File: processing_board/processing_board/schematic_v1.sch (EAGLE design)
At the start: 46 parts, among them Q1 BSS138, Q2 BSS138, Q3 BSS138, Q4 BSS138

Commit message: updated board
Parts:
- R13, R14, R15, R16, R17, R5, R6, R7, R8: value 10K -> 10k; device SparkFun-Resistors:220KOHM-0402T-1/16W-1% -> SparkFun-Resistors:10KOHM-0603-1/10W-1%
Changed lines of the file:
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@@
 <part name="D2" library="SparkFun-LED" deviceset="LED-GREEN" device="0603" value="GREEN"/>
 <part name="D3" library="SparkFun-LED" deviceset="LED-BLUE" device="0603" value="BLUE"/>
-<part name="R5" library="SparkFun-Resistors" deviceset="220KOHM" device="-0402T-1/16W-1%" value="10K"/>
-<part name="R6" library="SparkFun-Resistors" deviceset="220KOHM" device="-0402T-1/16W-1%" value="10K"/>
-<part name="R7" library="SparkFun-Resistors" deviceset="220KOHM" device="-0402T-1/16W-1%" value="10K"/>
+<part name="R5" library="SparkFun-Resistors" deviceset="10KOHM" device="-0603-1/10W-1%" value="10k"/>
+<part name="R6" library="SparkFun-Resistors" deviceset="10KOHM" device="-0603-1/10W-1%" value="10k"/>
+<part name="R7" library="SparkFun-Resistors" deviceset="10KOHM" device="-0603-1/10W-1%" value="10k"/>
 <part name="GND9" library="supply" deviceset="GND" device=""/>
 <part name="D4" library="SparkFun-LED" deviceset="LED-RED" device="0603" value="RED"/>
-<part name="R8" library="SparkFun-Resistors" deviceset="220KOHM" device="-0402T-1/16W-1%" value="10K"/>
+<part name="R8" library="SparkFun-Resistors" deviceset="10KOHM" device="-0603-1/10W-1%" value="10k"/>
 <part name="GND10" library="supply" deviceset="GND" device=""/>
 <part name="GND11" library="supply" deviceset="GND" device=""/>
@@
 <part name="PWR13" library="supply" deviceset="+5V" device=""/>
 <part name="D5" library="SparkFun-LED" deviceset="LED-GREEN" device="0603" value="GREEN"/>
-<part name="R13" library="SparkFun-Resistors" deviceset="220KOHM" device="-0402T-1/16W-1%" value="10K"/>
+<part name="R13" library="SparkFun-Resistors" deviceset="10KOHM" device="-0603-1/10W-1%" value="10k"/>
 <part name="PWR14" library="supply" deviceset="+3.3V" device=""/>
 <part name="PWR15" library="supply" deviceset="+5V" device=""/>
 <part name="D6" library="SparkFun-LED" deviceset="LED-GREEN" device="0603" value="GREEN"/>
-<part name="R14" library="SparkFun-Resistors" deviceset="220KOHM" device="-0402T-1/16W-1%" value="10K"/>
+<part name="R14" library="SparkFun-Resistors" deviceset="10KOHM" device="-0603-1/10W-1%" value="10k"/>
 <part name="D7" library="SparkFun-LED" deviceset="LED-GREEN" device="0603" value="GREEN"/>
-<part name="R15" library="SparkFun-Resistors" deviceset="220KOHM" device="-0402T-1/16W-1%" value="10K"/>
+<part name="R15" library="SparkFun-Resistors" deviceset="10KOHM" device="-0603-1/10W-1%" value="10k"/>
 <part name="PWR16" library="supply" deviceset="+3.3V" device=""/>
-<part name="R16" library="SparkFun-Resistors" deviceset="220KOHM" device="-0402T-1/16W-1%" value="10K"/>
+<part name="R16" library="SparkFun-Resistors" deviceset="10KOHM" device="-0603-1/10W-1%" value="10k"/>
 <part name="D8" library="SparkFun-LED" deviceset="LED-GREEN" device="0603" value="GREEN"/>
-<part name="R17" library="SparkFun-Resistors" deviceset="220KOHM" device="-0402T-1/16W-1%" value="10K"/>
+<part name="R17" library="SparkFun-Resistors" deviceset="10KOHM" device="-0603-1/10W-1%" value="10k"/>
 <part name="GND12" library="supply" deviceset="GND" device=""/>
 <part name="GND13" library="supply" deviceset="GND" device=""/>

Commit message: new teensy 4.1 footprint
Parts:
- removed U$1: DEV-16771, teensy_4_1:DEV-16771
- added B1: ARDUINO_UNO_R3, SparkFun-Boards:ARDUINO_UNO_R3
- added U$4: TEENSY41-E, teensy:TEENSY41-E
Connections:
- removed net N$9: JP1.10, U$1.D33
- new net N$15: U$4.37-PWM
- net +5V: now also U$4.VIN; no longer U$1.VIN
- net GND: now also U$4.5V, U$4.GND1, U$4.GND2, U$4.GND3, U$4.GND4, U$4.GND5, U$4.GND6; no longer U$1.AGND, U$1.GND, U$1.GND@1
- net N$1: now also U$4.35/TX8; no longer U$1.D35
- net N$11: now also U$4.1-TX1/MISO1/CTX2; no longer U$1.D1
- net N$2: now also U$4.34-RX8; no longer U$1.D34
- net N$5: now also U$4.0-RX1/CS1/CRX2; no longer U$1.D0
- net RESET_: now also JP1.10, U$4.33-MCLK2; no longer U$1.D36
- net SCL: now also U$4.16-A2/RX4/SCL1; no longer U$1.D19/A6
- net SDA: now also U$4.17-A3/TX4/SDA1; no longer U$1.D18/A5
- net TEENSY_3.3V: no longer U$1.3.3V
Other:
- moved on the sheet: C1, C2, C3, C4, C5, C6, D1, D2, D3, D4, D5, D8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

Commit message: pushing
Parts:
- added J5: (no value), SparkFun-Connectors:CONN_02
- added R18: 10k, SparkFun-Resistors:10KOHM-0603-1/10W-1%
- added R19: 8.2k, SparkFun-Resistors:8.2KOHM-0603-1/10W-5%
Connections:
- new net POWER_DIVIDED: R18.1, R19.2, U$4.27-A13/SCK1
- net +15V: now also R18.2
- net +5V: now also B1.VIN
- net CAN_RX1: now also J5.1
- net CAN_TX1: now also J5.2
- net GND: now also B1.GND, R19.1
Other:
- moved on the sheet: B1
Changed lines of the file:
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@@
 <part name="U$4" library="teensy" deviceset="TEENSY41-E" device=""/>
 <part name="B1" library="SparkFun-Boards" deviceset="ARDUINO_UNO_R3" device=""/>
+<part name="GND4" library="supply" deviceset="GND" device=""/>
+<part name="R18" library="SparkFun-Resistors" deviceset="10KOHM" device="-0603-1/10W-1%" value="10k"/>
+<part name="R19" library="SparkFun-Resistors" deviceset="8.2KOHM" device="-0603-1/10W-5%" value="8.2k"/>
+<part name="GND16" library="supply" deviceset="GND" device=""/>
+<part name="J5" library="SparkFun-Connectors" deviceset="CONN_02" device=""/>
 </parts>
 <sheets>
@@
 <instance part="GND15" gate="VR1" x="-147.32" y="-30.48" smashed="yes" rot="MR0"/>
 <instance part="U$4" gate="G$1" x="25.4" y="35.56" smashed="yes" rot="MR0"/>
-<instance part="B1" gate="G$1" x="142.24" y="-45.72" smashed="yes">
-<attribute name="NAME" x="132.588" y="-14.478" size="1.778" layer="95" font="vector"/>
-<attribute name="VALUE" x="132.08" y="-76.454" size="1.778" layer="96" font="vector" align="top-left"/>
+<instance part="B1" gate="G$1" x="142.24" y="58.42" smashed="yes">
+<attribute name="NAME" x="132.588" y="89.662" size="1.778" layer="95" font="vector"/>
+<attribute name="VALUE" x="132.08" y="27.686" size="1.778" layer="96" font="vector" align="top-left"/>
+</instance>
+<instance part="GND4" gate="VR1" x="116.84" y="30.48" smashed="yes" rot="R270"/>
+<instance part="R18" gate="G$1" x="137.16" y="165.1" smashed="yes" rot="R90">
+<attribute name="NAME" x="135.636" y="165.1" size="1.778" layer="95" font="vector" rot="R90" align="bottom-center"/>
+<attribute name="VALUE" x="138.684" y="165.1" size="1.778" layer="96" font="vector" rot="R90" align="top-center"/>
+</instance>
+<instance part="R19" gate="G$1" x="137.16" y="147.32" smashed="yes" rot="R90">
+<attribute name="NAME" x="135.636" y="147.32" size="1.778" layer="95" font="vector" rot="R90" align="bottom-center"/>
+<attribute name="VALUE" x="138.684" y="147.32" size="1.778" layer="96" font="vector" rot="R90" align="top-center"/>
+</instance>
+<instance part="GND16" gate="VR1" x="137.16" y="137.16" smashed="yes"/>
+<instance part="J5" gate="G$1" x="325.12" y="55.88" smashed="yes" rot="R180">
+<attribute name="VALUE" x="327.66" y="60.706" size="1.778" layer="96" font="vector" rot="R180"/>
+<attribute name="NAME" x="327.66" y="50.292" size="1.778" layer="95" font="vector" rot="R180"/>
 </instance>
 </instances>
@@
 <wire x1="-175.26" y1="-22.86" x2="-185.42" y2="-22.86" width="0.1524" layer="91"/>
 </segment>
+<segment>
+<pinref part="GND4" gate="VR1" pin="GND"/>
+<wire x1="119.38" y1="30.48" x2="129.54" y2="30.48" width="0.1524" layer="91"/>
+<label x="119.38" y="25.4" size="1.778" layer="95" rot="R180"/>
+<wire x1="129.54" y1="30.48" x2="130.81" y2="30.48" width="0.1524" layer="91"/>
+<junction x="129.54" y="30.48"/>
+<pinref part="B1" gate="G$1" pin="GND"/>
+</segment>
+<segment>
+<pinref part="GND16" gate="VR1" pin="GND"/>
+<wire x1="137.16" y1="142.24" x2="137.16" y2="139.7" width="0.1524" layer="91"/>
+<pinref part="R19" gate="G$1" pin="1"/>
+</segment>
 </net>
 <net name="+15V" class="0">
@@
 <wire x1="104.14" y1="167.64" x2="99.06" y2="167.64" width="0.1524" layer="91" grouprefs="POWER"/>
 <wire x1="99.06" y1="167.64" x2="99.06" y2="172.72" width="0.1524" layer="91" grouprefs="POWER"/>
+<wire x1="104.14" y1="167.64" x2="104.14" y2="175.26" width="0.1524" layer="91"/>
+<junction x="104.14" y="167.64"/>
+<wire x1="104.14" y1="175.26" x2="137.16" y2="175.26" width="0.1524" layer="91"/>
+<wire x1="137.16" y1="175.26" x2="137.16" y2="170.18" width="0.1524" layer="91"/>
+<pinref part="R18" gate="G$1" pin="2"/>
 </segment>
 <segment>
@@
 <pinref part="C2" gate="G$1" pin="1"/>
 <wire x1="80.518" y1="102.616" x2="73.66" y2="102.616" width="0.1524" layer="91"/>
-<wire x1="29.21" y1="83.82" x2="30.48" y2="83.82" width="0.1524" layer="91"/>
-<wire x1="30.48" y1="83.82" x2="73.66" y2="83.82" width="0.1524" layer="91"/>
+<wire x1="25.4" y1="83.82" x2="73.66" y2="83.82" width="0.1524" layer="91"/>
 <wire x1="73.66" y1="83.82" x2="73.66" y2="93.98" width="0.1524" layer="91"/>
 <wire x1="78.74" y1="83.82" x2="73.66" y2="83.82" width="0.1524" layer="91"/>
 <pinref part="U$4" gate="G$1" pin="VIN"/>
 <wire x1="25.4" y1="81.28" x2="25.4" y2="83.82" width="0.1524" layer="91"/>
-<wire x1="25.4" y1="83.82" x2="29.21" y2="83.82" width="0.1524" layer="91"/>
+<pinref part="B1" gate="G$1" pin="VIN"/>
+<wire x1="78.74" y1="83.82" x2="78.74" y2="63.5" width="0.1524" layer="91"/>
+<wire x1="78.74" y1="63.5" x2="129.54" y2="63.5" width="0.1524" layer="91"/>
+<junction x="78.74" y="83.82"/>
 </segment>
 <segment>
@@
 <junction x="266.7" y="53.34" grouprefs="I2C"/>
 <wire x1="248.92" y1="53.34" x2="248.92" y2="71.12" width="0.1524" layer="91" grouprefs="I2C"/>
+<wire x1="289.56" y1="53.34" x2="307.34" y2="53.34" width="0.1524" layer="91"/>
+<junction x="289.56" y="53.34"/>
+<pinref part="J5" gate="G$1" pin="1"/>
+<wire x1="307.34" y1="53.34" x2="307.34" y2="55.88" width="0.1524" layer="91"/>
+<wire x1="307.34" y1="55.88" x2="317.5" y2="55.88" width="0.1524" layer="91"/>
 </segment>
 </net>
@@
 <wire x1="256.54" y1="60.96" x2="256.54" y2="43.18" width="0.1524" layer="91"/>
 <junction x="256.54" y="43.18"/>
+<wire x1="289.56" y1="50.8" x2="309.88" y2="50.8" width="0.1524" layer="91"/>
+<junction x="289.56" y="50.8"/>
+<wire x1="309.88" y1="50.8" x2="309.88" y2="53.34" width="0.1524" layer="91"/>
+<pinref part="J5" gate="G$1" pin="2"/>
+<wire x1="309.88" y1="53.34" x2="317.5" y2="53.34" width="0.1524" layer="91"/>
 </segment>
 </net>
@@
 </segment>
 </net>
+<net name="POWER_DIVIDED" class="0">
+<segment>
+<pinref part="R19" gate="G$1" pin="2"/>
+<pinref part="R18" gate="G$1" pin="1"/>
+<wire x1="137.16" y1="152.4" x2="137.16" y2="154.94" width="0.1524" layer="91"/>
+<wire x1="137.16" y1="154.94" x2="137.16" y2="160.02" width="0.1524" layer="91"/>
+<wire x1="137.16" y1="154.94" x2="154.94" y2="154.94" width="0.1524" layer="91"/>
+<junction x="137.16" y="154.94"/>
+<label x="154.94" y="154.94" size="1.778" layer="95"/>
+</segment>
+<segment>
+<pinref part="U$4" gate="G$1" pin="27-A13/SCK1"/>
+<wire x1="55.88" y1="38.1" x2="63.5" y2="38.1" width="0.1524" layer="91"/>
+<label x="63.5" y="38.1" size="1.778" layer="95"/>
+<label x="63.5" y="38.1" size="1.778" layer="95"/>
+</segment>
+</net>

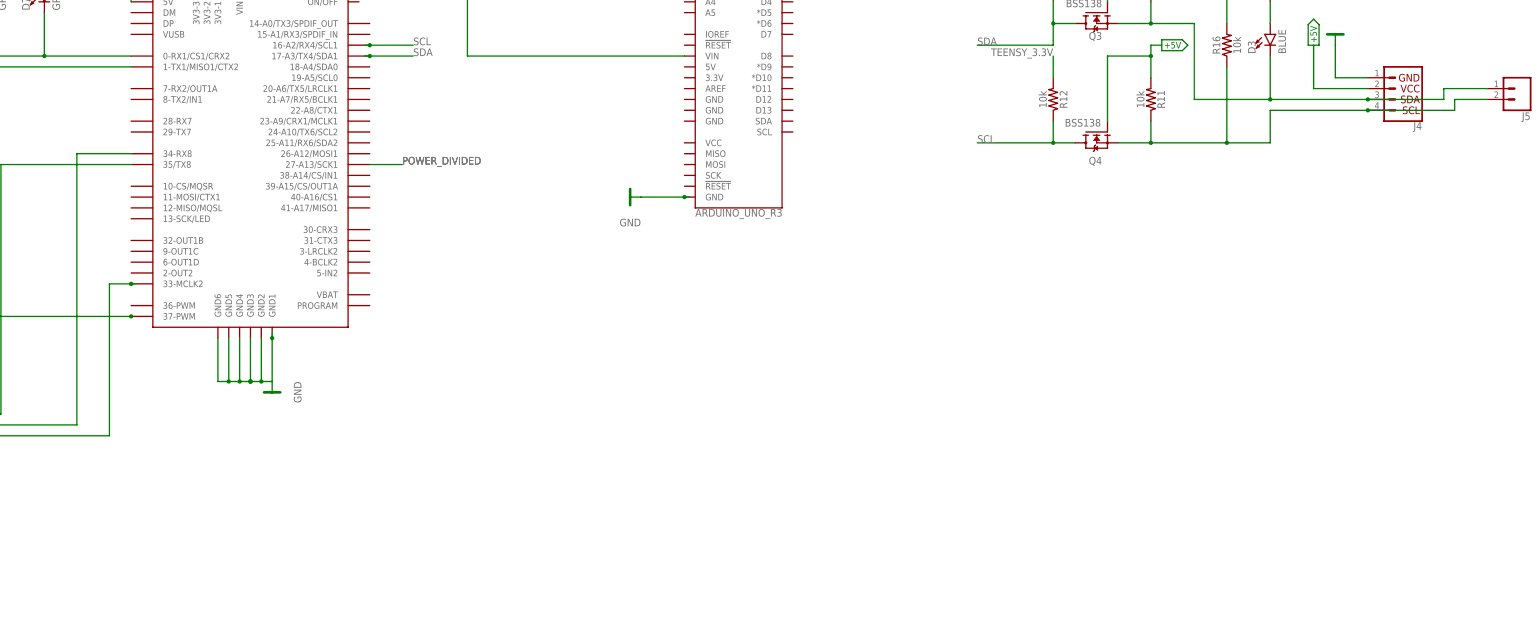
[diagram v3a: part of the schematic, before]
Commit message: added arduino headers
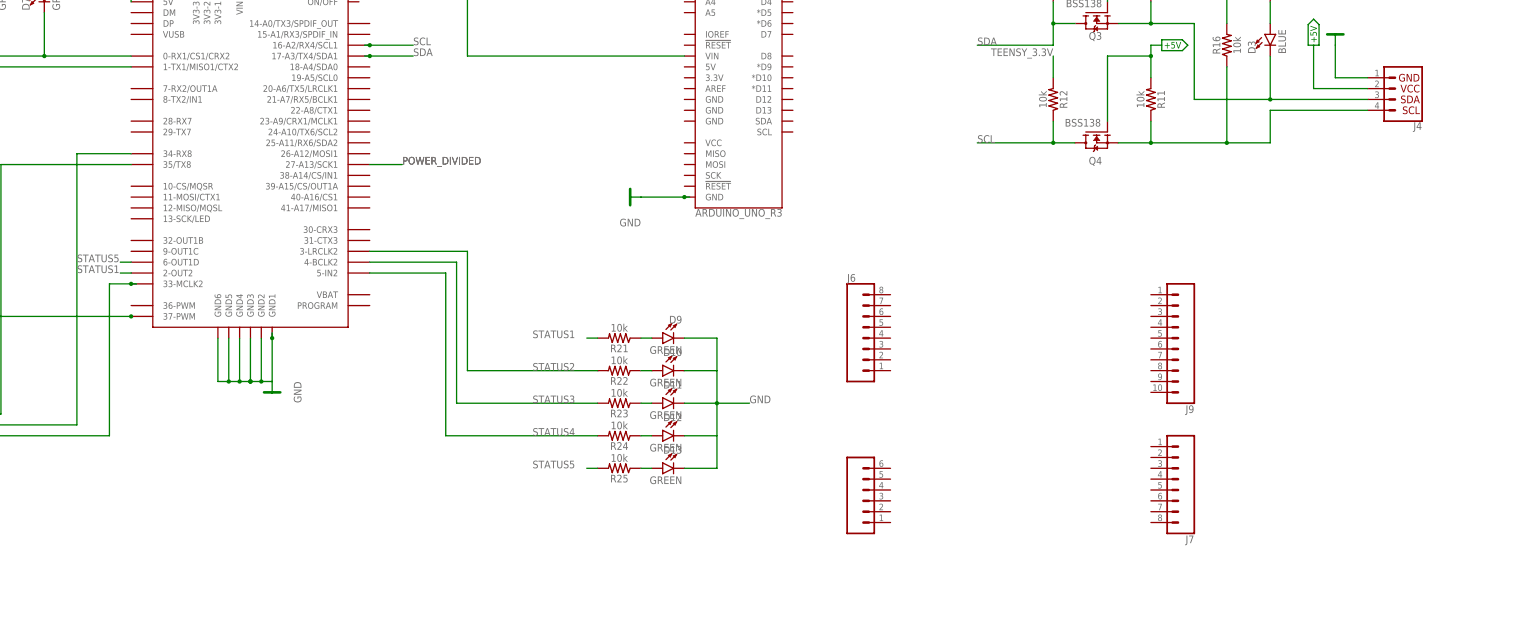
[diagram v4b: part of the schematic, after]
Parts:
- removed J5: (no value), SparkFun-Connectors:CONN_02
- added D10, D11, D12, D13, D9: GREEN, SparkFun-LED:LED-GREEN0603
- added J6, J7: (no value), SparkFun-Connectors:CONN_08NO_SILK_FEMALE_PTH
- added J8: (no value), SparkFun-Connectors:CONN_06SILK_FEMALE_PTH
- added J9: (no value), SparkFun-Connectors:CONN_10"
- added R21, R22, R23, R24, R25: 10k, SparkFun-Resistors:10KOHM-0603-1/10W-1%
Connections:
- new net N$16: D9.A, R21.1
- new net N$17: D10.C
- new net N$18: D10.A, R22.1
- new net N$20: D11.A, R23.1
- new net N$21: D12.C
- new net N$22: D12.A, R24.1
- new net N$24: D13.A, R25.1
- new net STATUS1: R21.2, U$4.2-OUT2
- new net STATUS2: R22.2, U$4.3-LRCLK2
- new net STATUS3: R23.2, U$4.4-BCLK2
- new net STATUS4: R24.2, U$4.5-IN2
- new net STATUS5: R25.2, U$4.6-OUT1D
- net CAN_RX1: no longer J5.1
- net CAN_TX1: no longer J5.2
- net GND: now also D11.C, D13.C, D9.C

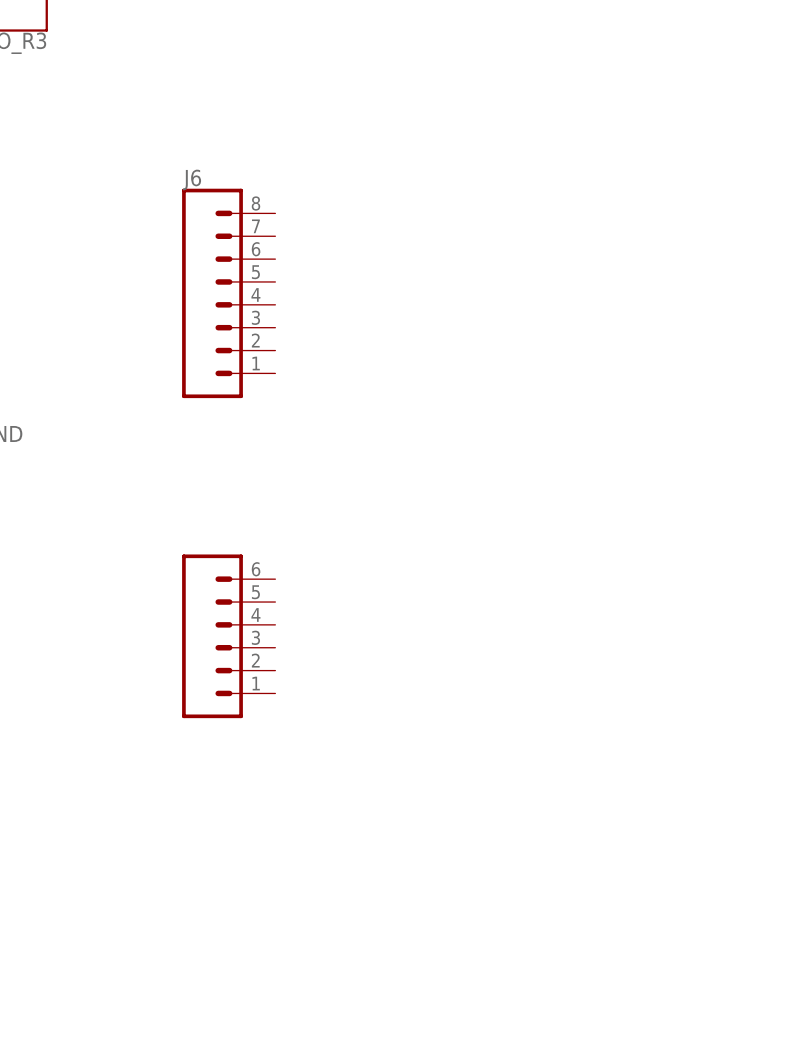
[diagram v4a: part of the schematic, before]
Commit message: added arduino pins
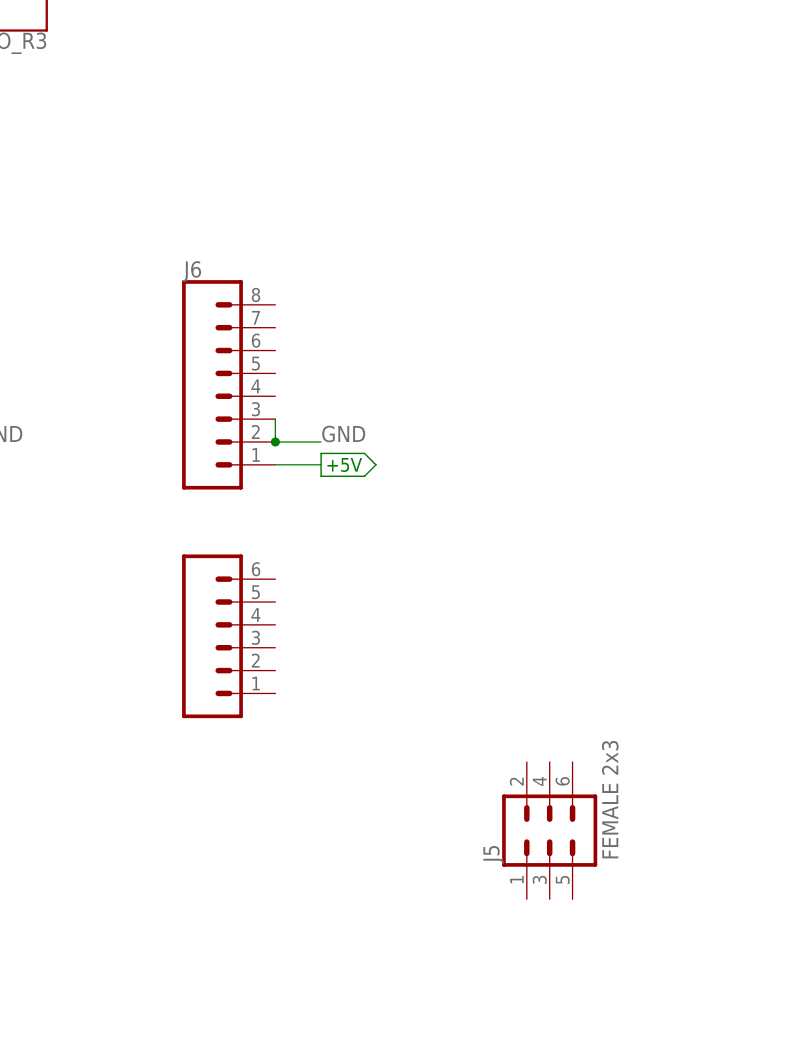
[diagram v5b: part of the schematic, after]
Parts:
- added J5: FEMALE 2x3, SparkFun-Connectors:CONN_03X2FEMALE
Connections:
- net +5V: now also J6.1
- net GND: now also J6.2, J6.3
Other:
- moved on the sheet: J6
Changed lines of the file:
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@@
 <part name="J7" library="SparkFun-Connectors" deviceset="CONN_08" device="NO_SILK_FEMALE_PTH"/>
 <part name="J9" library="SparkFun-Connectors" deviceset="CONN_10" device="&quot;"/>
+<part name="PWR17" library="supply" deviceset="+5V" device=""/>
+<part name="J5" library="SparkFun-Connectors" deviceset="CONN_03X2" device="FEMALE" value="FEMALE 2x3"/>
 </parts>
 <sheets>
@@
 <attribute name="VALUE" x="167.64" y="-50.546" size="1.778" layer="96" font="vector"/>
 </instance>
-<instance part="J6" gate="G$1" x="172.72" y="-2.54" smashed="yes">
-<attribute name="VALUE" x="167.64" y="-14.986" size="1.778" layer="96" font="vector"/>
-<attribute name="NAME" x="167.64" y="10.668" size="1.778" layer="95" font="vector"/>
+<instance part="J6" gate="G$1" x="172.72" y="-12.7" smashed="yes">
+<attribute name="VALUE" x="167.64" y="-25.146" size="1.778" layer="96" font="vector"/>
+<attribute name="NAME" x="167.64" y="0.508" size="1.778" layer="95" font="vector"/>
 </instance>
 <instance part="J7" gate="G$1" x="243.84" y="-35.56" smashed="yes" rot="R180">
@@
 <attribute name="VALUE" x="248.92" y="12.446" size="1.778" layer="96" font="vector" rot="R180"/>
 <attribute name="NAME" x="248.92" y="-18.288" size="1.778" layer="95" font="vector" rot="R180"/>
+</instance>
+<instance part="PWR17" gate="G$1" x="182.88" y="-20.32" smashed="yes" rot="R270"/>
+<instance part="J5" gate="G$1" x="208.28" y="-60.96" smashed="yes" rot="R90">
+<attribute name="NAME" x="202.692" y="-64.516" size="1.778" layer="95" font="vector" rot="R90"/>
+<attribute name="VALUE" x="214.122" y="-64.262" size="1.778" layer="96" font="vector" rot="R90" align="top-left"/>
 </instance>
 </instances>
@@
 <label x="144.78" y="-17.78" size="1.778" layer="95"/>
 </segment>
+<segment>
+<pinref part="J6" gate="G$1" pin="3"/>
+<pinref part="J6" gate="G$1" pin="2"/>
+<wire x1="177.8" y1="-15.24" x2="177.8" y2="-17.78" width="0.1524" layer="91"/>
+<wire x1="177.8" y1="-17.78" x2="182.88" y2="-17.78" width="0.1524" layer="91"/>
+<junction x="177.8" y="-17.78"/>
+<label x="182.88" y="-17.78" size="1.778" layer="95"/>
+</segment>
 </net>
 <net name="+15V" class="0">
@@
 <junction x="266.7" y="86.36"/>
 </segment>
+<segment>
+<pinref part="J6" gate="G$1" pin="1"/>
+<wire x1="177.8" y1="-20.32" x2="182.88" y2="-20.32" width="0.1524" layer="91"/>
+<pinref part="PWR17" gate="G$1" pin="+5V"/>
+</segment>
 </net>
